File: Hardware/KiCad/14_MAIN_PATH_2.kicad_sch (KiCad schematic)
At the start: 0 parts

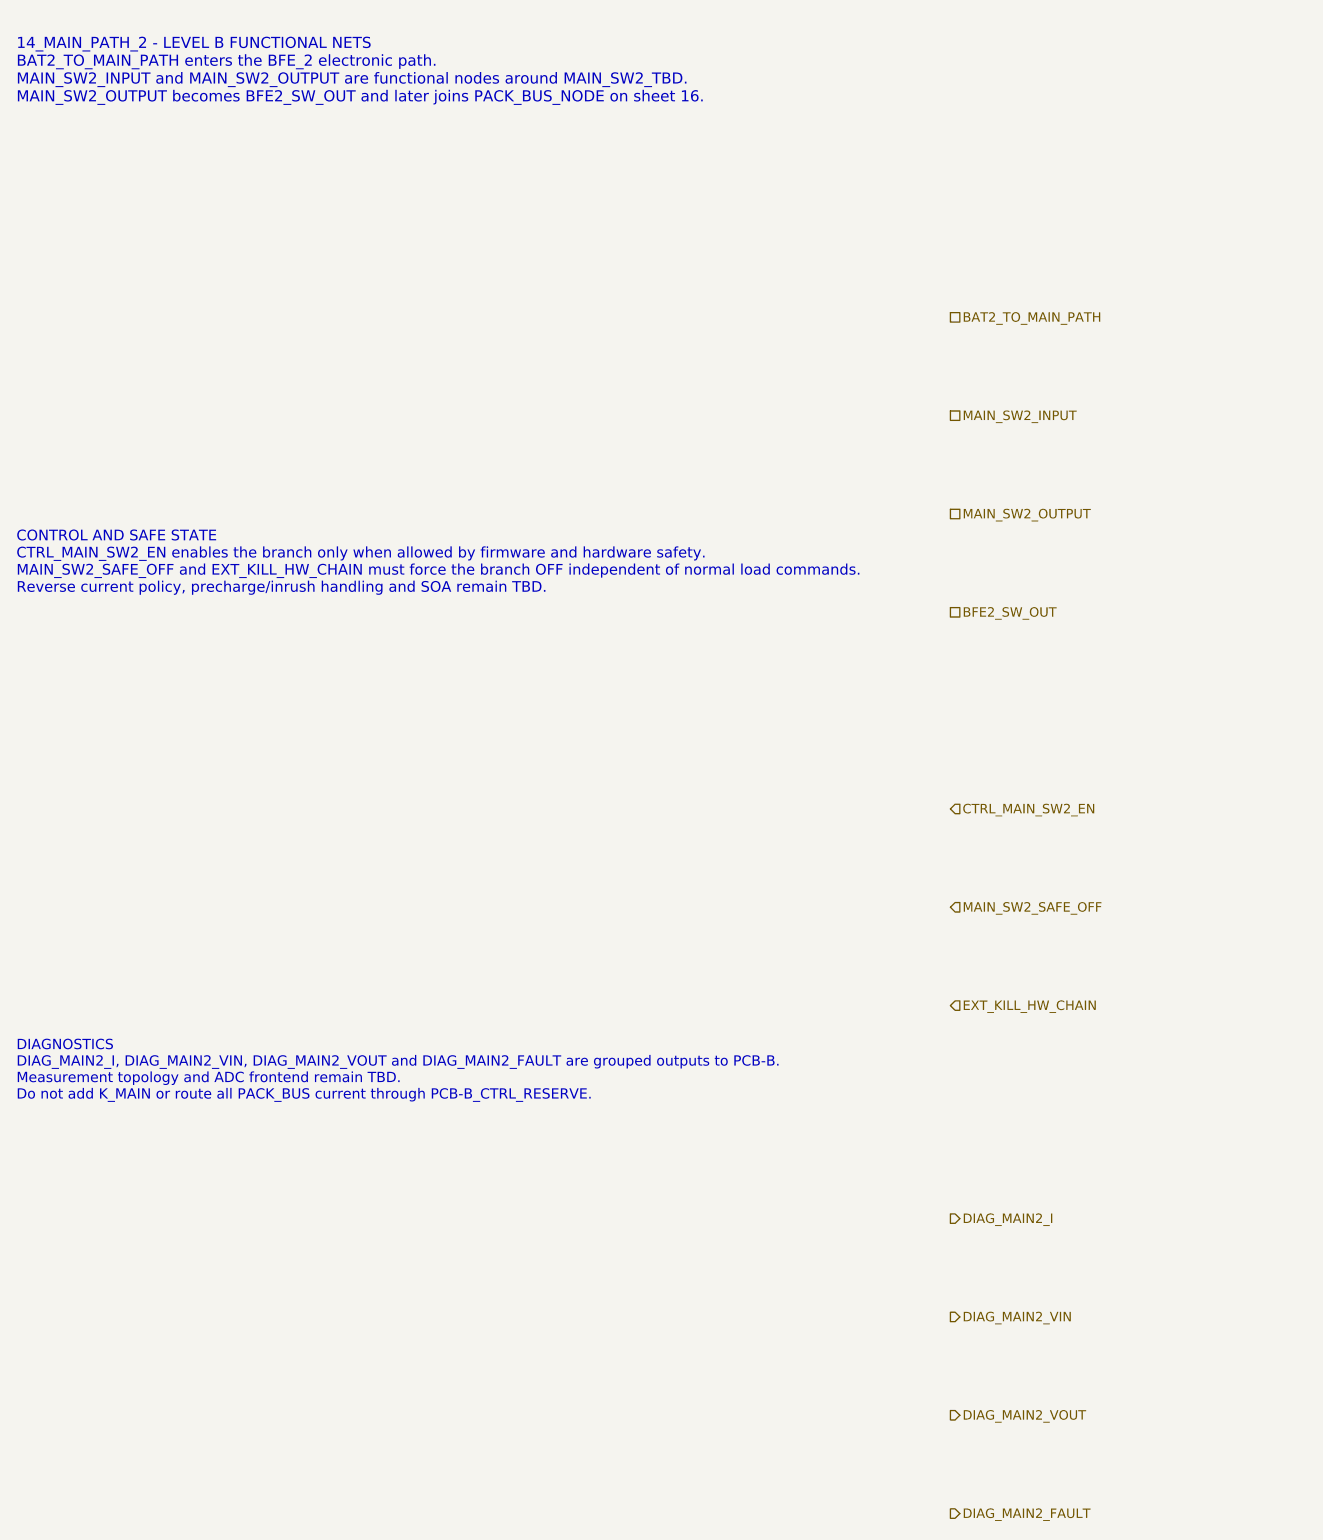
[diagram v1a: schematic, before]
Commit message: hardware: add MAIN_SW2 symbol skeleton zones
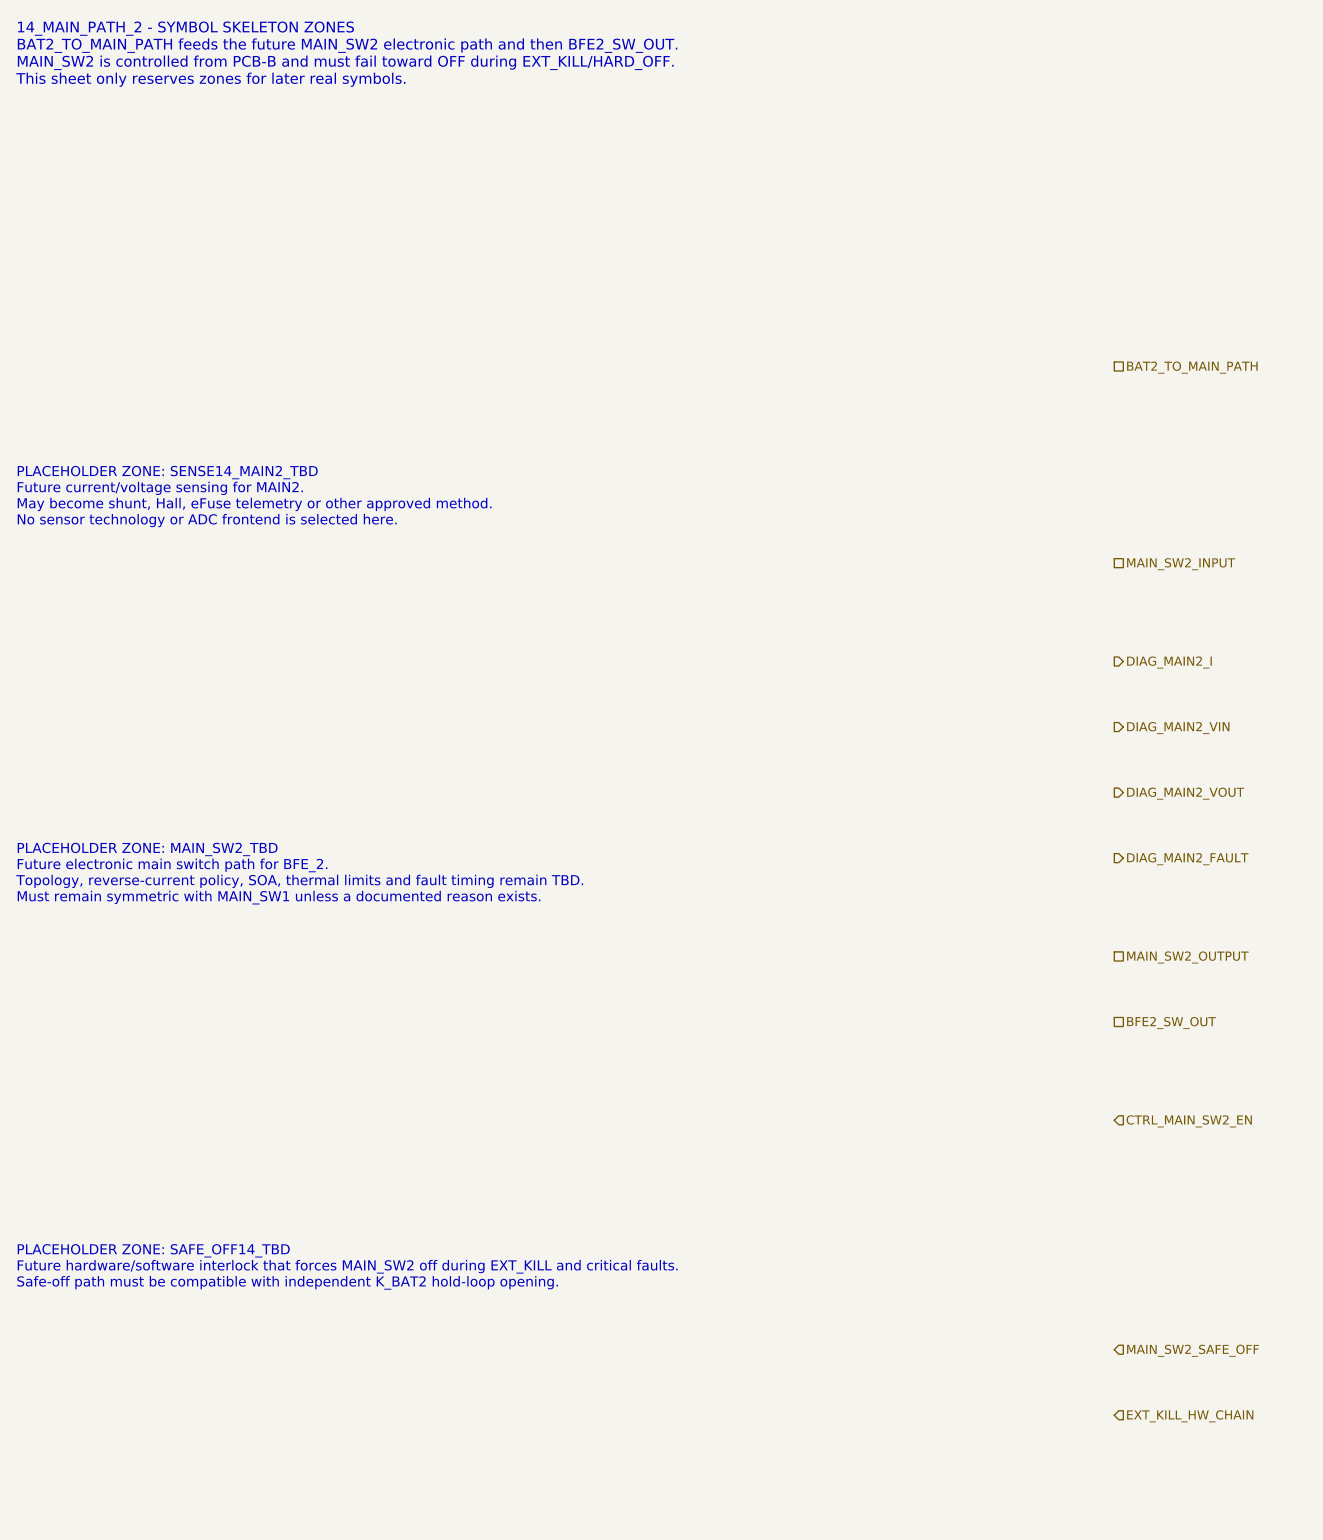
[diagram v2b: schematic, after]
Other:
- note added: "14_MAIN_PATH_2 - SYMBOL SKELETON ZONES BAT2_TO_MAIN_PATH feeds the future MAIN_SW2 electronic path and then BFE2_SW_OUT. MAIN_SW2 is controlled from PCB-B and must fail toward OFF during EXT_KILL/HARD_OFF. This sheet only reserves zones for later real symbols."
- note added: "PLACEHOLDER ZONE: MAIN_SW2_TBD Future electronic main switch path for BFE_2. Topology, reverse-current policy, SOA, thermal limits and fault timing remain TBD. Must remain symmetric with MAIN_SW1 unless a documented reason exists."
- note added: "PLACEHOLDER ZONE: SAFE_OFF14_TBD Future hardware/software interlock that forces MAIN_SW2 off during EXT_KILL and critical faults. Safe-off path must be compatible with independent K_BAT2 hold-loop opening."
- note added: "PLACEHOLDER ZONE: SENSE14_MAIN2_TBD Future current/voltage sensing for MAIN2. May become shunt, Hall, eFuse telemetry or other approved method. No sensor technology or ADC frontend is selected here."
- note removed: "14_MAIN_PATH_2 - LEVEL B FUNCTIONAL NETS BAT2_TO_MAIN_PATH enters the BFE_2 electronic path. MAIN_SW2_INPUT and MAIN_SW2_OUTPUT are functional nodes around MAIN_SW2_TBD. MAIN_SW2_OUTPUT becomes BFE2_SW_OUT and later joins PACK_BUS_NODE on sheet 16."
- note removed: "CONTROL AND SAFE STATE CTRL_MAIN_SW2_EN enables the branch only when allowed by firmware and hardware safety. MAIN_SW2_SAFE_OFF and EXT_KILL_HW_CHAIN must force the branch OFF independent of normal load commands. Reverse current policy, precharge/inrush handling and SOA remain TBD."
- note removed: "DIAGNOSTICS DIAG_MAIN2_I, DIAG_MAIN2_VIN, DIAG_MAIN2_VOUT and DIAG_MAIN2_FAULT are grouped outputs to PCB-B. Measurement topology and ADC frontend remain TBD. Do not add K_MAIN or route all PACK_BUS current through PCB-B_CTRL_RESERVE."
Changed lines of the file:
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@@
 		(title "14_MAIN_PATH_2 - BFE_2 main electronic path")
 		(date "2026-07-15")
-		(rev "B1")
+		(rev "C1")
 		(company "Gonoboben/plataVM")
-		(comment 1 "Architecture Level B: MAIN_SW2 control, diagnostics and safe-state nets")
-		(comment 2 "Symmetric to 13_MAIN_PATH_1; no MAIN_SW2 topology selected")
+		(comment 1 "Symbol skeleton: MAIN_SW2, sensing and safe-off placeholders")
+		(comment 2 "Symmetric to 13_MAIN_PATH_1; no topology, footprint or component selected")
 	)
-	(text "14_MAIN_PATH_2 - LEVEL B FUNCTIONAL NETS\nBAT2_TO_MAIN_PATH enters the BFE_2 electronic path.\nMAIN_SW2_INPUT and MAIN_SW2_OUTPUT are functional nodes around MAIN_SW2_TBD.\nMAIN_SW2_OUTPUT becomes BFE2_SW_OUT and later joins PACK_BUS_NODE on sheet 16."
+	(text "14_MAIN_PATH_2 - SYMBOL SKELETON ZONES\nBAT2_TO_MAIN_PATH feeds the future MAIN_SW2 electronic path and then BFE2_SW_OUT.\nMAIN_SW2 is controlled from PCB-B and must fail toward OFF during EXT_KILL/HARD_OFF.\nThis sheet only reserves zones for later real symbols."
 		(exclude_from_sim no)
-		(at 12 18 0)
-		(effects (font (size 1.35 1.35)) (justify left))
+		(at 12 16 0)
+		(effects (font (size 1.3 1.3)) (justify left))
 		(uuid "bfe-lb-00000014-0000-4000-8000-000000000101")
 	)
-	(text "CONTROL AND SAFE STATE\nCTRL_MAIN_SW2_EN enables the branch only when allowed by firmware and hardware safety.\nMAIN_SW2_SAFE_OFF and EXT_KILL_HW_CHAIN must force the branch OFF independent of normal load commands.\nReverse current policy, precharge/inrush handling and SOA remain TBD."
+	(text "PLACEHOLDER ZONE: SENSE14_MAIN2_TBD\nFuture current/voltage sensing for MAIN2.\nMay become shunt, Hall, eFuse telemetry or other approved method.\nNo sensor technology or ADC frontend is selected here."
 		(exclude_from_sim no)
-		(at 12 78 0)
-		(effects (font (size 1.3 1.3)) (justify left))
+		(at 12 70 0)
+		(effects (font (size 1.22 1.22)) (justify left))
 		(uuid "bfe-lb-00000014-0000-4000-8000-000000000102")
 	)
-	(text "DIAGNOSTICS\nDIAG_MAIN2_I, DIAG_MAIN2_VIN, DIAG_MAIN2_VOUT and DIAG_MAIN2_FAULT are grouped outputs to PCB-B.\nMeasurement topology and ADC frontend remain TBD.\nDo not add K_MAIN or route all PACK_BUS current through PCB-B_CTRL_RESERVE."
+	(text "PLACEHOLDER ZONE: MAIN_SW2_TBD\nFuture electronic main switch path for BFE_2.\nTopology, reverse-current policy, SOA, thermal limits and fault timing remain TBD.\nMust remain symmetric with MAIN_SW1 unless a documented reason exists."
 		(exclude_from_sim no)
-		(at 12 140 0)
-		(effects (font (size 1.25 1.25)) (justify left))
+		(at 12 116 0)
+		(effects (font (size 1.22 1.22)) (justify left))
 		(uuid "bfe-lb-00000014-0000-4000-8000-000000000103")
 	)
-	(hierarchical_label "BAT2_TO_MAIN_PATH" (shape passive) (exclude_from_sim no) (at 126 48 0) (effects (font (size 1.15 1.15)) (justify left)) (uuid "bfe-lb-00000014-0000-4000-8000-000000000201"))
-	(hierarchical_label "MAIN_SW2_INPUT" (shape passive) (exclude_from_sim no) (at 126 60 0) (effects (font (size 1.15 1.15)) (justify left)) (uuid "bfe-lb-00000014-0000-4000-8000-000000000202"))
-	(hierarchical_label "MAIN_SW2_OUTPUT" (shape passive) (exclude_from_sim no) (at 126 72 0) (effects (font (size 1.15 1.15)) (justify left)) (uuid "bfe-lb-00000014-0000-4000-8000-000000000203"))
-	(hierarchical_label "BFE2_SW_OUT" (shape passive) (exclude_from_sim no) (at 126 84 0) (effects (font (size 1.15 1.15)) (justify left)) (uuid "bfe-lb-00000014-0000-4000-8000-000000000204"))
-	(hierarchical_label "CTRL_MAIN_SW2_EN" (shape input) (exclude_from_sim no) (at 126 108 0) (effects (font (size 1.15 1.15)) (justify left)) (uuid "bfe-lb-00000014-0000-4000-8000-000000000205"))
-	(hierarchical_label "MAIN_SW2_SAFE_OFF" (shape input) (exclude_from_sim no) (at 126 120 0) (effects (font (size 1.15 1.15)) (justify left)) (uuid "bfe-lb-00000014-0000-4000-8000-000000000206"))
-	(hierarchical_label "EXT_KILL_HW_CHAIN" (shape input) (exclude_from_sim no) (at 126 132 0) (effects (font (size 1.15 1.15)) (justify left)) (uuid "bfe-lb-00000014-0000-4000-8000-000000000207"))
-	(hierarchical_label "DIAG_MAIN2_I" (shape output) (exclude_from_sim no) (at 126 158 0) (effects (font (size 1.15 1.15)) (justify left)) (uuid "bfe-lb-00000014-0000-4000-8000-000000000208"))
-	(hierarchical_label "DIAG_MAIN2_VIN" (shape output) (exclude_from_sim no) (at 126 170 0) (effects (font (size 1.15 1.15)) (justify left)) (uuid "bfe-lb-00000014-0000-4000-8000-000000000209"))
-	(hierarchical_label "DIAG_MAIN2_VOUT" (shape output) (exclude_from_sim no) (at 126 182 0) (effects (font (size 1.15 1.15)) (justify left)) (uuid "bfe-lb-00000014-0000-4000-8000-000000000210"))
-	(hierarchical_label "DIAG_MAIN2_FAULT" (shape output) (exclude_from_sim no) (at 126 194 0) (effects (font (size 1.15 1.15)) (justify left)) (uuid "bfe-lb-00000014-0000-4000-8000-000000000211"))
+	(text "PLACEHOLDER ZONE: SAFE_OFF14_TBD\nFuture hardware/software interlock that forces MAIN_SW2 off during EXT_KILL and critical faults.\nSafe-off path must be compatible with independent K_BAT2 hold-loop opening."
+		(exclude_from_sim no)
+		(at 12 164 0)
+		(effects (font (size 1.22 1.22)) (justify left))
+		(uuid "bfe-lb-00000014-0000-4000-8000-000000000104")
+	)
+	(hierarchical_label "BAT2_TO_MAIN_PATH" (shape passive) (exclude_from_sim no) (at 146 54 0) (effects (font (size 1.1 1.1)) (justify left)) (uuid "bfe-lb-00000014-0000-4000-8000-000000000201"))
+	(hierarchical_label "MAIN_SW2_INPUT" (shape passive) (exclude_from_sim no) (at 146 78 0) (effects (font (size 1.1 1.1)) (justify left)) (uuid "bfe-lb-00000014-0000-4000-8000-000000000202"))
+	(hierarchical_label "MAIN_SW2_OUTPUT" (shape passive) (exclude_from_sim no) (at 146 126 0) (effects (font (size 1.1 1.1)) (justify left)) (uuid "bfe-lb-00000014-0000-4000-8000-000000000203"))
+	(hierarchical_label "BFE2_SW_OUT" (shape passive) (exclude_from_sim no) (at 146 134 0) (effects (font (size 1.1 1.1)) (justify left)) (uuid "bfe-lb-00000014-0000-4000-8000-000000000204"))
+	(hierarchical_label "CTRL_MAIN_SW2_EN" (shape input) (exclude_from_sim no) (at 146 146 0) (effects (font (size 1.1 1.1)) (justify left)) (uuid "bfe-lb-00000014-0000-4000-8000-000000000205"))
+	(hierarchical_label "MAIN_SW2_SAFE_OFF" (shape input) (exclude_from_sim no) (at 146 174 0) (effects (font (size 1.1 1.1)) (justify left)) (uuid "bfe-lb-00000014-0000-4000-8000-000000000206"))
+	(hierarchical_label "EXT_KILL_HW_CHAIN" (shape input) (exclude_from_sim no) (at 146 182 0) (effects (font (size 1.1 1.1)) (justify left)) (uuid "bfe-lb-00000014-0000-4000-8000-000000000207"))
+	(hierarchical_label "DIAG_MAIN2_I" (shape output) (exclude_from_sim no) (at 146 90 0) (effects (font (size 1.1 1.1)) (justify left)) (uuid "bfe-lb-00000014-0000-4000-8000-000000000208"))
+	(hierarchical_label "DIAG_MAIN2_VIN" (shape output) (exclude_from_sim no) (at 146 98 0) (effects (font (size 1.1 1.1)) (justify left)) (uuid "bfe-lb-00000014-0000-4000-8000-000000000209"))
+	(hierarchical_label "DIAG_MAIN2_VOUT" (shape output) (exclude_from_sim no) (at 146 106 0) (effects (font (size 1.1 1.1)) (justify left)) (uuid "bfe-lb-00000014-0000-4000-8000-000000000210"))
+	(hierarchical_label "DIAG_MAIN2_FAULT" (shape output) (exclude_from_sim no) (at 146 114 0) (effects (font (size 1.1 1.1)) (justify left)) (uuid "bfe-lb-00000014-0000-4000-8000-000000000211"))
 )
